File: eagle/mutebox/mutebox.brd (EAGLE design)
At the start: 127 x 63.5 mm, 39 parts

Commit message: mutebox
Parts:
- added C7, C8: 100nF, microbuilder:0603
- added IC1: 74HCT595D, 74xx-eu:SO16
- added IC2: 74HC165D, 74xx-eu:SO16
- added JP4: (no value), pinhead:2X06
- added JP5: (no value), microbuilder:1X03_ROUND
- added R17, R18, R19, R20, R21, R22, R23, R24: 220, microbuilder:_0603
- added R25, R26, R27, R28, R29, R30, R31, R32: 10K, microbuilder:_0603
- JP1: device pinhead:2X10 -> pinhead:2X06
- moved JP1 117.1 mm to (121.4, 31.0), flipped to the top, turned to 90 degrees
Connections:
- removed net P10-: JP1.12
- removed net P11-: JP1.13
- removed net P12-: JP1.14
- removed net P13-: JP1.15
- removed net P14-: JP1.16
- removed net P15-: JP1.17
- removed net P16-: JP1.18
- removed net P9-: JP1.11
- new net B_LED1: IC1.15, R17.1
- new net B_LED2: IC1.1, R18.1
- new net B_LED3: IC1.2, R19.1
- new net B_LED4: IC1.3, R20.1
- new net B_LED5: IC1.4, R21.1
- new net B_LED6: IC1.5, R22.1
- new net B_LED7: IC1.6, R23.1
- new net B_LED8: IC1.7, R24.1
- new net B_PB1: IC2.6, R25.1, U$1.P3
- new net B_PB2: IC2.5, R26.1, U$2.P3
- new net B_PB3: IC2.4, R27.1, U$3.P3
- new net B_PB4: IC2.3, R28.1, U$4.P3
- new net B_PB5: IC2.14, R29.1, U$5.P3
- new net B_PB6: IC2.13, R30.1, U$6.P3
- new net B_PB7: IC2.12, R31.1, U$7.P3
- new net B_PB8: IC2.11, R32.1, U$8.P3
- new net B_RC: IC1.12, IC2.1, JP5.2
- new net B_RC_1: JP1.7, JP1.8, JP5.1
- new net B_RC_2: JP1.10, JP1.9, JP5.3
- new net B_SC: IC1.11, IC2.2, JP1.5, JP1.6
- new net B_SO: IC1.14, JP1.3, JP1.4
- new net GND: C7.1, C8.1, IC1.13, IC1.8, IC2.15, IC2.8, JP1.11, JP1.12, U$1.LED-, U$1.P1, U$2.LED-, U$2.P1, U$3.LED-, U$3.P1, U$4.LED-, U$4.P1, U$5.LED-, U$5.P1, U$6.LED-, U$6.P1, U$7.LED-, U$7.P1, U$8.LED-, U$8.P1
- new net N$1: R17.2, U$1.LED+
- new net N$2: R18.2, U$2.LED+
- new net N$3: R19.2, U$3.LED+
- new net N$4: R20.2, U$4.LED+
- new net N$5: R21.2, U$5.LED+
- new net N$6: R22.2, U$6.LED+
- new net N$7: R23.2, U$7.LED+
- new net N$8: R24.2, U$8.LED+
- new net N$9: IC1.9, IC2.9
- new net VCC: C7.2, C8.2, IC1.10, IC1.16, IC2.16, JP1.1, JP1.2, R25.2, R26.2, R27.2, R28.2, R29.2, R30.2, R31.2, R32.2
- net AGND: now also JP4.11, JP4.12; no longer JP1.19, JP1.20
- net AVCC: now also JP4.1, JP4.2; no longer JP1.1, JP1.2
- net P_CLK: now also JP4.10, JP4.9; no longer JP1.10, JP1.9
- net P_CS1: now also JP4.4; no longer JP1.3
- net P_CS2: now also JP4.3; no longer JP1.4
- net P_CS3: now also JP4.6; no longer JP1.5
- net P_CS4: now also JP4.5; no longer JP1.6
- net P_DIN: now also JP4.8; no longer JP1.7
- net P_DOUT: now also JP4.7; no longer JP1.8
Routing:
- net VCC: track 0.00 -> 9.34 mm, vias 0 -> 2
- net N$2: track 0.00 -> 2.09 mm
- net N$7: track 0.00 -> 2.08 mm
- net N$6: track 0.00 -> 2.08 mm
- net N$1: track 0.00 -> 1.84 mm
- net N$5: track 0.00 -> 1.82 mm
- net N$4: track 0.00 -> 1.82 mm
- net N$8: track 0.00 -> 1.67 mm
- added copper zone on layer 16, net GND
- added copper zone on layer 1, net VCC

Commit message: mutebox
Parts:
- removed JP5: (no value), microbuilder:1X03_ROUND
- moved IC1 0.57 mm to (5.84, 17.8)
- moved C7 0.57 mm to (2.79, 24.9)
- moved R32 0.51 mm to (115.6, 5.33)
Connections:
- removed net B_RC_1: JP1.7, JP1.8, JP5.1
- removed net B_RC_2: JP1.10, JP1.9, JP5.3
- removed net N$9: IC1.9, IC2.9
- new net B_SI: IC2.9, JP1.10, JP1.9
- net B_LED1: now also IC1.4; no longer IC1.15
- net B_LED2: now also IC1.3; no longer IC1.1
- net B_LED4: now also IC1.1; no longer IC1.3
- net B_LED5: now also IC1.15; no longer IC1.4
- net B_PB3: now also IC2.3; no longer IC2.4
- net B_PB4: now also IC2.4; no longer IC2.3
- net B_RC: now also JP1.7, JP1.8; no longer JP5.2
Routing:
- net B_RC: track 0.00 -> 155.3 mm, vias 0 -> 2
- net B_SC: track 0.00 -> 145.5 mm, vias 0 -> 2
- net B_SO: track 0.00 -> 133.6 mm, vias 0 -> 1
- net B_PB1: track 0.00 -> 125.8 mm, vias 0 -> 1
- net B_PB2: track 0.00 -> 109.3 mm, vias 0 -> 1
- net B_LED8: track 0.00 -> 105.9 mm
- net B_LED7: track 0.00 -> 95.5 mm
- net B_PB3: track 0.00 -> 84.1 mm, vias 0 -> 2
- net B_LED6: track 0.00 -> 80.0 mm
- net B_PB4: track 0.00 -> 74.0 mm, vias 0 -> 2
- net B_LED5: track 0.00 -> 72.5 mm
- net B_PB5: track 0.00 -> 59.6 mm, vias 0 -> 2
- net B_LED4: track 0.00 -> 51.4 mm
- net B_PB6: track 0.00 -> 51.2 mm
- net B_PB7: track 0.00 -> 39.4 mm
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
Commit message: mutebox
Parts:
- removed JP2, JP3: (no value), microbuilder:1X03_ROUND
- moved JP1 0.92 mm to (121.9, 31.8)
- moved JP4 0.25 mm to (5.08, 47.0)
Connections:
- removed net P_CS3: JP3.1, JP4.6
- removed net P_CS4: JP3.3, JP4.5
- removed net P_CS_A: JP2.2, U$29.P$10
- removed net P_CS_B: JP3.2, U$47.P$10
- net P_CLK: now also JP4.7, JP4.8; no longer JP4.10, JP4.9
- net P_CS1: now also U$29.P$10; no longer JP2.1
- net P_CS2: now also U$47.P$10; no longer JP2.3
- net P_DIN: now also JP4.6; no longer JP4.8
- net P_DOUT: now also JP4.5; no longer JP4.7
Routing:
- net P_CS2: track 11.1 -> 91.2 mm, vias 0 -> 1
- net P_CS_B: track 77.7 -> 0.00 mm, vias 1 -> 0
- net P_CS3: track 21.2 -> 0.00 mm
- net P_CS_A: track 21.1 -> 0.00 mm
- net P_CS1: track 13.6 -> 33.9 mm
- net P_CS4: track 16.9 -> 0.00 mm
- net P_CLK: track 108.4 -> 107.0 mm
- net B_SO: track 133.6 -> 134.6 mm
- net P_DOUT: track 106.6 -> 106.0 mm

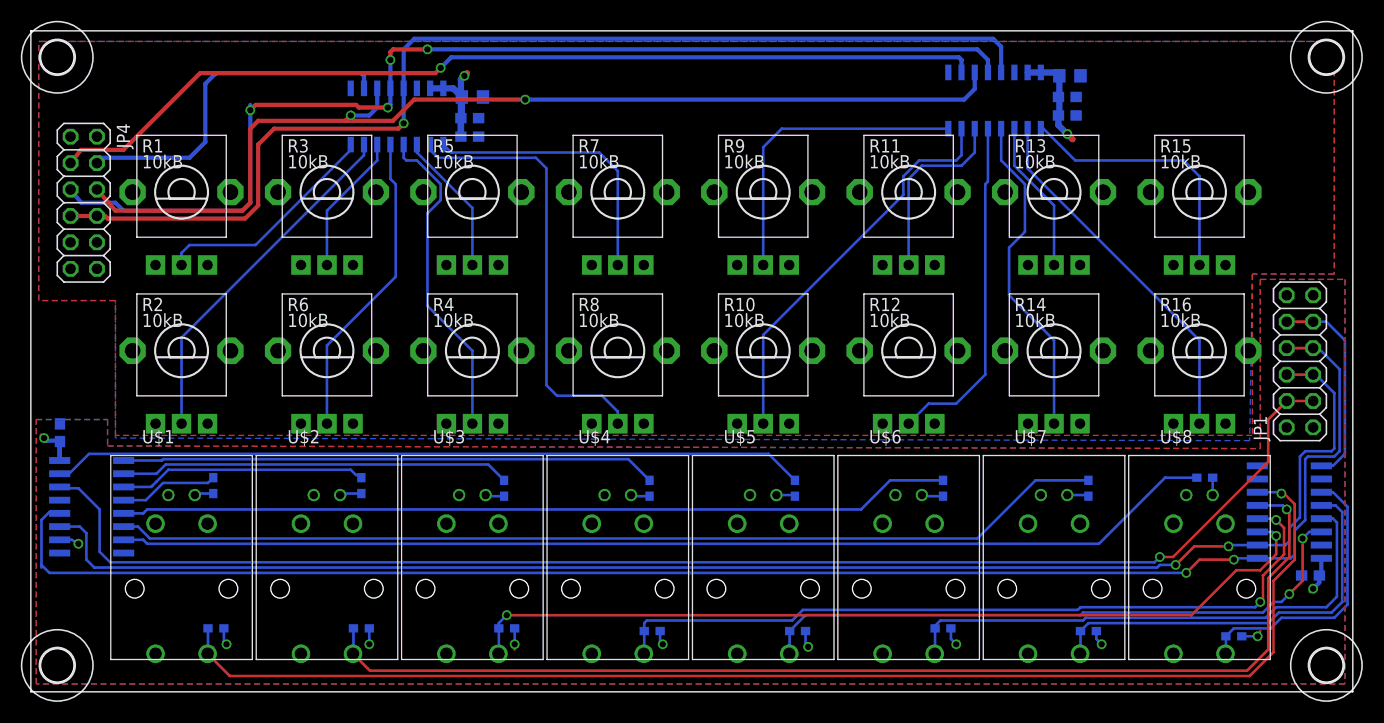
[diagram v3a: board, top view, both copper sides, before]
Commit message: mutebox: connectors now match midibox
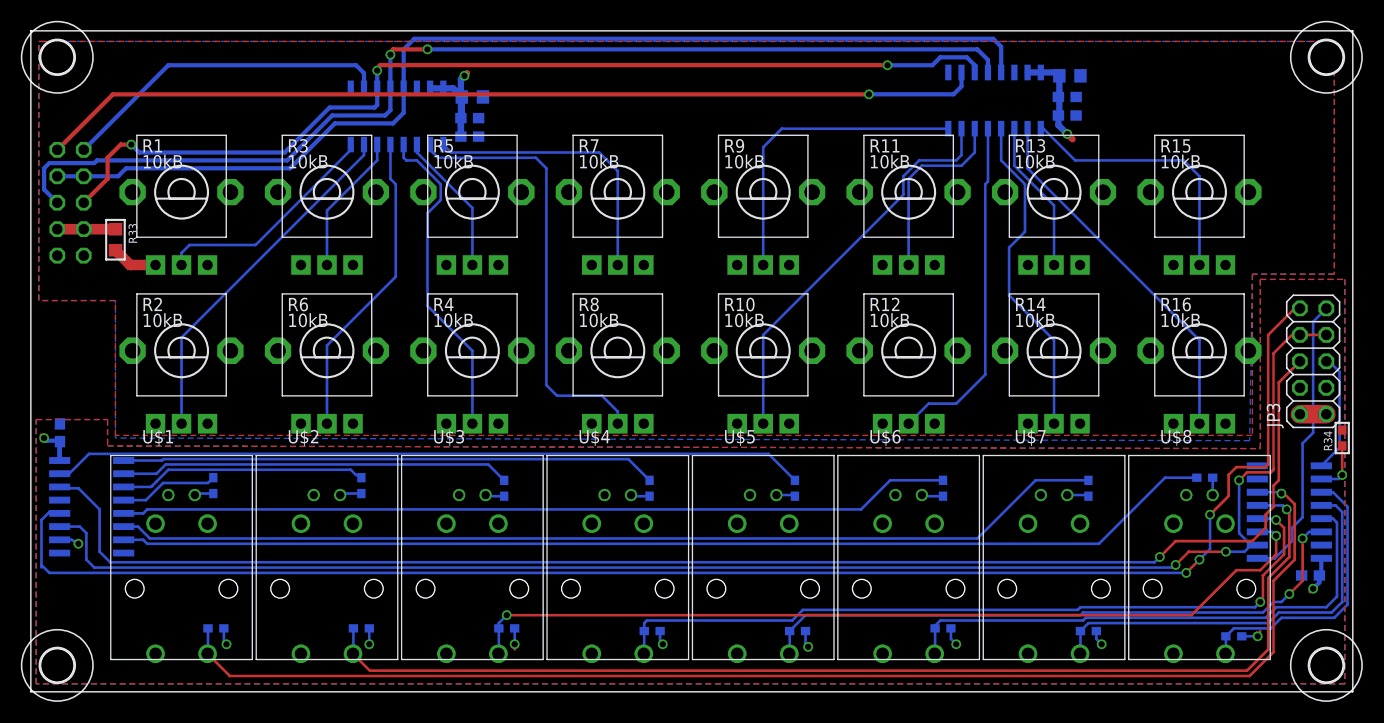
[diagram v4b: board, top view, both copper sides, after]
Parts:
- removed JP1, JP4: (no value), pinhead:2X06
- added JP2, JP3: (no value), pinhead:2X05
- added R33: 10, microbuilder:_0805
- added R34: 10K, microbuilder:_0603
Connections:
- removed net B_RC: IC1.12, IC2.1, JP1.7, JP1.8
- new net B_RC1: IC2.1, JP3.9
- new net B_RC2: IC1.12, JP3.10
- new net N$10: IC2.10, R34.1
- new net N$9: JP2.3, JP2.4, R33.1
- net AGND: now also JP2.1, JP2.2; no longer JP4.11, JP4.12
- net AVCC: now also R33.2; no longer JP4.1, JP4.2
- net B_SC: now also JP3.7, JP3.8; no longer JP1.5, JP1.6
- net B_SI: now also JP3.5; no longer JP1.10, JP1.9
- net B_SO: now also JP3.6; no longer JP1.3, JP1.4
- net GND: now also JP3.1, JP3.2; no longer JP1.11, JP1.12
- net P_CLK: now also JP2.7, JP2.8; no longer JP4.7, JP4.8
- net P_CS1: now also JP2.10; no longer JP4.4
- net P_CS2: now also JP2.9; no longer JP4.3
- net P_DIN: now also JP2.6; no longer JP4.6
- net P_DOUT: now also JP2.5; no longer JP4.5
- net VCC: now also JP3.3, JP3.4, R34.2; no longer JP1.1, JP1.2
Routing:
- net B_RC: track 155.1 -> 0.00 mm, vias 2 -> 0
- net B_RC2: track 0.00 -> 148.8 mm, vias 0 -> 3
- net B_RC1: track 0.00 -> 27.7 mm
- net B_SI: track 20.0 -> 11.4 mm
- net N$9: track 0.00 -> 5.59 mm
- net B_SO: track 134.6 -> 140.0 mm
- net P_DIN: track 101.3 -> 96.3 mm, vias 2 -> 3
- net N$10: track 0.00 -> 4.96 mm, vias 0 -> 1
- net P_CLK: track 107.0 -> 102.5 mm, vias 1 -> 0
- net AVCC: track 23.6 -> 28.0 mm
- net GND: track 0.00 -> 2.54 mm
- net P_DOUT: track 106.0 -> 104.1 mm, vias 4 -> 2
- net P_CS1: track 33.9 -> 32.1 mm
- net B_SC: track 145.3 -> 146.7 mm, vias 2 -> 3

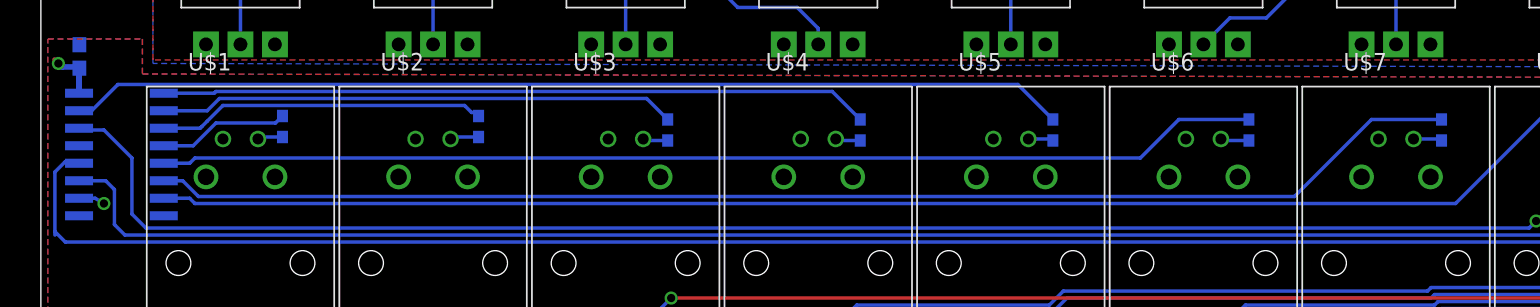
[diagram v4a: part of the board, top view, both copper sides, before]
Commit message: mutebox: rearranged leds
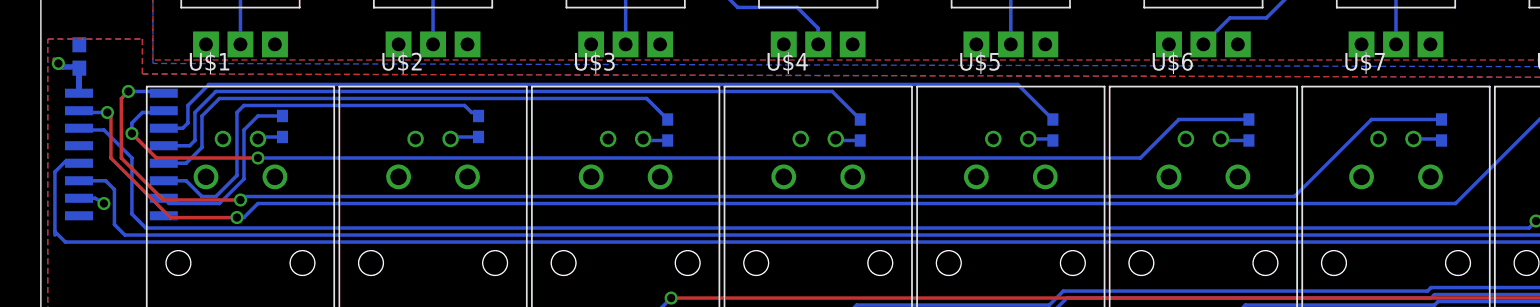
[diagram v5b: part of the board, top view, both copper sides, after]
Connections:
- net B_LED1: now also IC1.7; no longer IC1.4
- net B_LED2: now also IC1.6; no longer IC1.3
- net B_LED3: now also IC1.5; no longer IC1.2
- net B_LED4: now also IC1.4; no longer IC1.1
- net B_LED5: now also IC1.3; no longer IC1.15
- net B_LED6: now also IC1.2; no longer IC1.5
- net B_LED7: now also IC1.1; no longer IC1.6
- net B_LED8: now also IC1.15; no longer IC1.7
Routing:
- net B_LED7: track 95.5 -> 107.1 mm, vias 0 -> 2
- net B_LED8: track 105.9 -> 117.3 mm, vias 0 -> 2
- net B_LED6: track 80.0 -> 86.4 mm, vias 0 -> 2
- net B_LED2: track 23.8 -> 29.0 mm
- net B_LED5: track 72.5 -> 67.6 mm
- net B_LED1: track 9.50 -> 13.7 mm
- net B_LED3: track 37.6 -> 40.5 mm
- net B_LED4: track 51.4 -> 54.2 mm
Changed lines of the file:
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@@
 <signal name="B_LED1">
 <contactref element="R17" pad="1"/>
-<contactref element="IC1" pad="4"/>
-<wire x1="8.9154" y1="18.415" x2="11.049" y2="18.415" width="0.254" layer="16"/>
-<wire x1="11.049" y1="18.415" x2="12.7" y2="20.066" width="0.254" layer="16"/>
-<wire x1="12.7" y1="20.066" x2="17.018" y2="20.066" width="0.254" layer="16"/>
-<wire x1="17.018" y1="20.066" x2="17.526" y2="20.574" width="0.254" layer="16"/>
+<contactref element="IC1" pad="7"/>
+<wire x1="15.748" y1="20.574" x2="17.526" y2="20.574" width="0.254" layer="16"/>
+<wire x1="14.732" y1="16.002" x2="14.732" y2="19.558" width="0.254" layer="16"/>
+<wire x1="14.732" y1="19.558" x2="15.748" y2="20.574" width="0.254" layer="16"/>
+<wire x1="14.732" y1="16.002" x2="12.954" y2="14.224" width="0.254" layer="16"/>
+<wire x1="9.0424" y1="14.478" x2="8.9154" y2="14.605" width="0.254" layer="16"/>
+<wire x1="12.954" y1="14.224" x2="9.2964" y2="14.224" width="0.254" layer="16"/>
+<wire x1="9.2964" y1="14.224" x2="8.9154" y2="14.605" width="0.254" layer="16"/>
 </signal>
 <signal name="B_LED2">
 <contactref element="R18" pad="1"/>
-<contactref element="IC1" pad="3"/>
 <wire x1="31.75" y1="20.574" x2="31.496" y2="20.828" width="0.254" layer="16"/>
 <wire x1="31.496" y1="20.828" x2="31.242" y2="20.828" width="0.254" layer="16"/>
 <wire x1="31.242" y1="20.828" x2="30.734" y2="21.336" width="0.254" layer="16"/>
-<wire x1="30.734" y1="21.336" x2="13.208" y2="21.336" width="0.254" layer="16"/>
-<wire x1="13.208" y1="21.336" x2="12.065" y2="20.193" width="0.254" layer="16"/>
-<wire x1="12.065" y1="20.193" x2="11.684" y2="19.812" width="0.254" layer="16"/>
-<wire x1="8.9154" y1="19.685" x2="11.557" y2="19.685" width="0.254" layer="16"/>
-<wire x1="11.557" y1="19.685" x2="11.684" y2="19.812" width="0.254" layer="16"/>
+<wire x1="30.734" y1="21.336" x2="14.732" y2="21.336" width="0.254" layer="16"/>
+<contactref element="IC1" pad="6"/>
+<wire x1="8.9154" y1="15.875" x2="10.541" y2="15.875" width="0.254" layer="16"/>
+<wire x1="10.541" y1="15.875" x2="11.684" y2="14.732" width="0.254" layer="16"/>
+<wire x1="12.7" y1="14.732" x2="14.224" y2="16.256" width="0.254" layer="16"/>
+<wire x1="14.224" y1="16.256" x2="14.224" y2="20.828" width="0.254" layer="16"/>
+<wire x1="14.224" y1="20.828" x2="14.732" y2="21.336" width="0.254" layer="16"/>
+<wire x1="11.684" y1="14.732" x2="12.7" y2="14.732" width="0.254" layer="16"/>
 </signal>
 <signal name="B_LED3">
 <contactref element="R19" pad="1"/>
-<contactref element="IC1" pad="2"/>
-<wire x1="8.9154" y1="20.955" x2="12.065" y2="20.955" width="0.254" layer="16"/>
-<wire x1="12.065" y1="20.955" x2="12.954" y2="21.844" width="0.254" layer="16"/>
 <wire x1="12.954" y1="21.844" x2="43.942" y2="21.844" width="0.254" layer="16"/>
 <wire x1="43.942" y1="21.844" x2="45.466" y2="20.32" width="0.254" layer="16"/>
+<contactref element="IC1" pad="5"/>
+<wire x1="8.9154" y1="17.145" x2="10.541" y2="17.145" width="0.254" layer="16"/>
+<wire x1="10.541" y1="17.145" x2="11.684" y2="18.288" width="0.254" layer="16"/>
+<wire x1="11.684" y1="18.288" x2="11.684" y2="20.574" width="0.254" layer="16"/>
+<wire x1="11.684" y1="20.574" x2="12.954" y2="21.844" width="0.254" layer="16"/>
 </signal>
 <signal name="B_LED4">
 <contactref element="R20" pad="1"/>
-<contactref element="IC1" pad="1"/>
-<wire x1="8.9154" y1="22.225" x2="12.573" y2="22.225" width="0.254" layer="16"/>
-<wire x1="12.573" y1="22.225" x2="12.7" y2="22.352" width="0.254" layer="16"/>
 <wire x1="12.7" y1="22.352" x2="57.404" y2="22.352" width="0.254" layer="16"/>
 <wire x1="57.404" y1="22.352" x2="59.436" y2="20.32" width="0.254" layer="16"/>
+<contactref element="IC1" pad="4"/>
+<wire x1="8.9154" y1="18.415" x2="10.795" y2="18.415" width="0.254" layer="16"/>
+<wire x1="10.795" y1="18.415" x2="11.176" y2="18.796" width="0.254" layer="16"/>
+<wire x1="11.176" y1="18.796" x2="11.176" y2="20.828" width="0.254" layer="16"/>
+<wire x1="11.176" y1="20.828" x2="12.7" y2="22.352" width="0.254" layer="16"/>
 </signal>
 <signal name="B_LED5">
 <contactref element="R21" pad="1"/>
-<contactref element="IC1" pad="15"/>
-<wire x1="2.7686" y1="20.955" x2="3.683" y2="20.955" width="0.254" layer="16"/>
-<wire x1="3.683" y1="20.955" x2="5.588" y2="22.86" width="0.254" layer="16"/>
-<wire x1="5.588" y1="22.86" x2="70.866" y2="22.86" width="0.254" layer="16"/>
+<wire x1="12.192" y1="22.86" x2="70.866" y2="22.86" width="0.254" layer="16"/>
 <wire x1="70.866" y1="22.86" x2="73.406" y2="20.32" width="0.254" layer="16"/>
+<contactref element="IC1" pad="3"/>
+<wire x1="8.9154" y1="19.685" x2="10.287" y2="19.685" width="0.254" layer="16"/>
+<wire x1="10.287" y1="19.685" x2="10.668" y2="20.066" width="0.254" layer="16"/>
+<wire x1="10.668" y1="20.066" x2="10.668" y2="21.336" width="0.254" layer="16"/>
+<wire x1="10.668" y1="21.336" x2="12.192" y2="22.86" width="0.254" layer="16"/>
 </signal>
 <signal name="B_LED6">
 <contactref element="R22" pad="1"/>
-<contactref element="IC1" pad="5"/>
-<wire x1="8.9154" y1="17.145" x2="10.795" y2="17.145" width="0.254" layer="16"/>
-<wire x1="10.795" y1="17.145" x2="11.176" y2="17.526" width="0.254" layer="16"/>
-<wire x1="11.176" y1="17.526" x2="79.756" y2="17.526" width="0.254" layer="16"/>
+<wire x1="15.748" y1="17.526" x2="79.756" y2="17.526" width="0.254" layer="16"/>
 <wire x1="79.756" y1="17.526" x2="82.55" y2="20.32" width="0.254" layer="16"/>
 <wire x1="82.55" y1="20.32" x2="87.63" y2="20.32" width="0.254" layer="16"/>
+<contactref element="IC1" pad="2"/>
+<via x="15.748" y="17.526" extent="1-16" drill="0.6"/>
+<wire x1="15.748" y1="17.526" x2="8.382" y2="17.526" width="0.254" layer="1"/>
+<wire x1="8.382" y1="17.526" x2="6.604" y2="19.304" width="0.254" layer="1"/>
+<via x="6.604" y="19.304" extent="1-16" drill="0.6"/>
+<wire x1="6.604" y1="19.304" x2="6.604" y2="20.066" width="0.254" layer="16"/>
+<wire x1="6.604" y1="20.066" x2="7.366" y2="20.828" width="0.254" layer="16"/>
+<wire x1="7.366" y1="20.828" x2="8.7884" y2="20.828" width="0.254" layer="16"/>
+<wire x1="8.7884" y1="20.828" x2="8.9154" y2="20.955" width="0.254" layer="16"/>
 </signal>
 <signal name="B_LED7">
 <contactref element="R23" pad="1"/>
-<contactref element="IC1" pad="6"/>
-<wire x1="8.9154" y1="15.875" x2="10.287" y2="15.875" width="0.254" layer="16"/>
-<wire x1="10.287" y1="15.875" x2="11.43" y2="14.732" width="0.254" layer="16"/>
-<wire x1="11.43" y1="14.732" x2="90.932" y2="14.732" width="0.254" layer="16"/>
+<wire x1="14.732" y1="14.732" x2="90.932" y2="14.732" width="0.254" layer="16"/>
 <wire x1="90.932" y1="14.732" x2="96.52" y2="20.32" width="0.254" layer="16"/>
 <wire x1="96.52" y1="20.32" x2="101.6" y2="20.32" width="0.254" layer="16"/>
+<contactref element="IC1" pad="1"/>
+<wire x1="14.732" y1="14.732" x2="14.478" y2="14.478" width="0.254" layer="16"/>
+<via x="14.478" y="14.478" extent="1-16" drill="0.6"/>
+<wire x1="14.478" y1="14.478" x2="8.89" y2="14.478" width="0.254" layer="1"/>
+<wire x1="8.89" y1="14.478" x2="5.842" y2="17.526" width="0.254" layer="1"/>
+<wire x1="5.842" y1="17.526" x2="5.842" y2="21.844" width="0.254" layer="1"/>
+<wire x1="5.842" y1="21.844" x2="6.35" y2="22.352" width="0.254" layer="1"/>
+<via x="6.35" y="22.352" extent="1-16" drill="0.6"/>
+<wire x1="6.35" y1="22.352" x2="8.7884" y2="22.352" width="0.254" layer="16"/>
+<wire x1="8.7884" y1="22.352" x2="8.9154" y2="22.225" width="0.254" layer="16"/>
 </signal>
 <signal name="B_LED8">
 <contactref element="R24" pad="1"/>
-<contactref element="IC1" pad="7"/>
-<wire x1="8.9154" y1="14.605" x2="10.795" y2="14.605" width="0.254" layer="16"/>
-<wire x1="10.795" y1="14.605" x2="11.176" y2="14.224" width="0.254" layer="16"/>
-<wire x1="11.176" y1="14.224" x2="102.616" y2="14.224" width="0.254" layer="16"/>
+<wire x1="15.748" y1="14.224" x2="102.616" y2="14.224" width="0.254" layer="16"/>
 <wire x1="102.616" y1="14.224" x2="108.966" y2="20.574" width="0.254" layer="16"/>
 <wire x1="108.966" y1="20.574" x2="112.014" y2="20.574" width="0.254" layer="16"/>
+<contactref element="IC1" pad="15"/>
+<via x="14.224" y="13.208" extent="1-16" drill="0.6"/>
+<wire x1="14.224" y1="13.208" x2="9.398" y2="13.208" width="0.254" layer="1"/>
+<wire x1="9.398" y1="13.208" x2="5.08" y2="17.526" width="0.254" layer="1"/>
+<wire x1="5.08" y1="17.526" x2="5.08" y2="20.574" width="0.254" layer="1"/>
+<wire x1="5.08" y1="20.574" x2="4.826" y2="20.828" width="0.254" layer="1"/>
+<via x="4.826" y="20.828" extent="1-16" drill="0.6"/>
+<wire x1="4.826" y1="20.828" x2="2.8956" y2="20.828" width="0.254" layer="16"/>
+<wire x1="2.8956" y1="20.828" x2="2.7686" y2="20.955" width="0.254" layer="16"/>
+<wire x1="14.224" y1="13.208" x2="14.732" y2="13.208" width="0.254" layer="16"/>
+<wire x1="14.732" y1="13.208" x2="15.748" y2="14.224" width="0.254" layer="16"/>
 </signal>
 <signal name="VCC">
@@
 <contactref element="JP2" pad="4"/>
 <contactref element="JP2" pad="3"/>
+<wire x1="5.08" y1="44.45" x2="2.54" y2="44.45" width="1.016" layer="1"/>
 <wire x1="8.128" y1="44.45" x2="5.08" y2="44.45" width="1.016" layer="1"/>
-<wire x1="5.08" y1="44.45" x2="2.54" y2="44.45" width="1.016" layer="1"/>
 </signal>
 <signal name="B_RC2">
